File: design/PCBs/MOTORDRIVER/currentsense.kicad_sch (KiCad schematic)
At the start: 0 parts

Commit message: updated PCB
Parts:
- added U5: INA180A1, Package_TO_SOT_SMD:SOT-23-5, symbol Amplifier_Current:INA180A1
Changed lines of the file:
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@@
 	(paper "A4")
 	(rectangle
-		(start 105.41 74.93)
-		(end 162.56 116.84)
+		(start 68.326 64.008)
+		(end 125.476 105.918)
 		(stroke
 			(width 0)
@@
 	(text "Current sensor IC\nTODO: Find component"
 		(exclude_from_sim no)
-		(at 132.334 98.552 0)
+		(at 95.25 87.63 0)
 		(effects
 			(font
@@
 			)
 		)
+	)
+	(symbol
+		(lib_id "Amplifier_Current:INA180A1")
+		(at 153.67 105.41 0)
+		(unit 1)
+		(exclude_from_sim no)
+		(in_bom yes)
+		(on_board yes)
+		(dnp no)
+		(fields_autoplaced yes)
+		(property "Reference" "U5"
+			(at 163.83 98.4755 0)
+			(effects
+				(font
+					(size 1.27 1.27)
+				)
+			)
+		)
+		(property "Value" "INA180A1"
+			(at 163.83 101.0155 0)
+			(effects
+				(font
+					(size 1.27 1.27)
+				)
+			)
+		)
+		(property "Footprint" "Package_TO_SOT_SMD:SOT-23-5"
+			(at 154.94 104.14 0)
+			(effects
+				(font
+					(size 1.27 1.27)
+				)
+				(hide yes)
+			)
+		)
+		(property "Datasheet" "http://www.ti.com/lit/ds/symlink/ina180.pdf"
+			(at 157.48 101.6 0)
+			(effects
+				(font
+					(size 1.27 1.27)
+				)
+				(hide yes)
+			)
+		)
+		(property "Description" "Current Sense Amplifier, 1 Circuit, Rail-to-Rail, 26V, Gain 20 V/V, SOT-23-5"
+			(at 153.67 105.41 0)
+			(effects
+				(font
+					(size 1.27 1.27)
+				)
+				(hide yes)
+			)
+		)
+		(pin "3"
+		)
+		(pin "2"
+		)
+		(pin "1"
+		)
+		(pin "5"
+		)
+		(pin "4"
+		)
+		(instances
+			(project ""
+				(path "/c7634e88-16d1-45ec-9aac-9c841e03cf6d/22c06531-1f6c-46f3-988e-cea008e98016"
+					(reference "U5")
+					(unit 1)
+				)
+				(path "/c7634e88-16d1-45ec-9aac-9c841e03cf6d/474d6285-5514-49ae-8177-1e63fd9cd03e"
+					(reference "U7")
+					(unit 1)
+				)
+				(path "/c7634e88-16d1-45ec-9aac-9c841e03cf6d/721caf15-f1fc-41df-88f3-9bb14360f09a"
+					(reference "U6")
+					(unit 1)
+				)
+			)
+		)

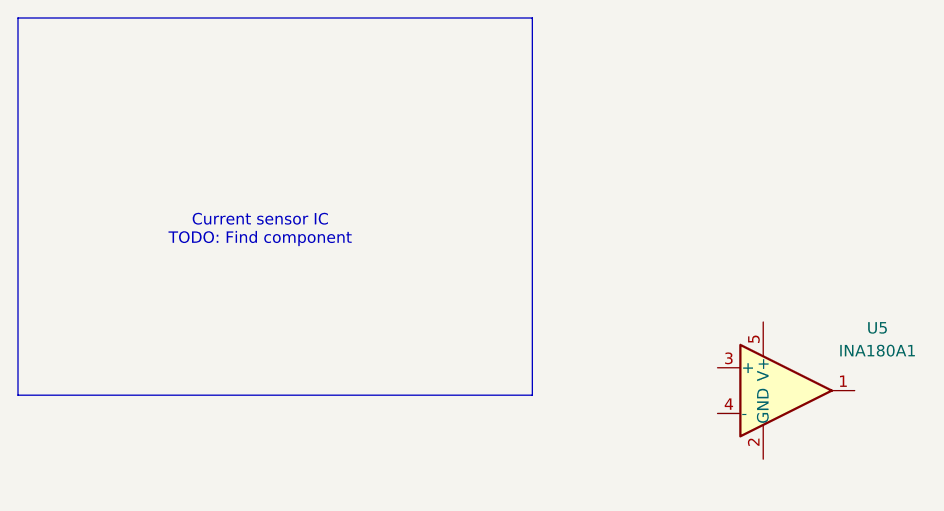
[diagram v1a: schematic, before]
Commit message: fixed schematic layout and added shunt resistor and zener diodes for motor stage
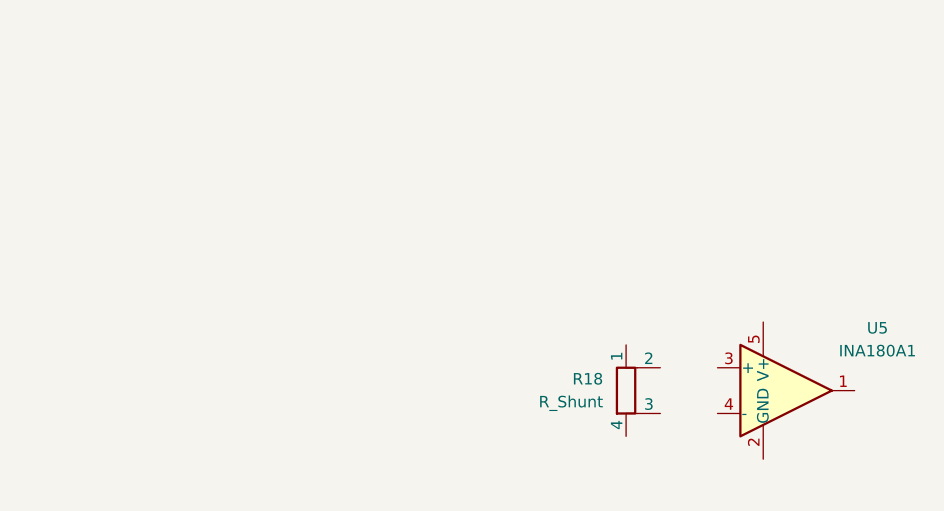
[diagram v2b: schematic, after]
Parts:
- added R18: R_Shunt, symbol Device:R_Shunt
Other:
- note removed: "Current sensor IC TODO: Find component"
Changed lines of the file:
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@@
 	(generator_version "8.0")
 	(paper "A4")
-	(rectangle
-		(start 68.326 64.008)
-		(end 125.476 105.918)
-		(stroke
-			(width 0)
-			(type default)
-		)
-		(fill
-			(type none)
-		)
-	)
-	(text "Current sensor IC\nTODO: Find component"
+	(symbol
+		(lib_id "Device:R_Shunt")
+		(at 135.89 105.41 0)
+		(unit 1)
 		(exclude_from_sim no)
-		(at 95.25 87.63 0)
-		(effects
-			(font
-				(size 1.27 1.27)
+		(in_bom yes)
+		(on_board yes)
+		(dnp no)
+		(fields_autoplaced yes)
+		(property "Reference" "R18"
+			(at 133.35 104.1399 0)
+			(effects
+				(font
+					(size 1.27 1.27)
+				)
+				(justify right)
 			)
 		)
+		(property "Value" "R_Shunt"
+			(at 133.35 106.6799 0)
+			(effects
+				(font
+					(size 1.27 1.27)
+				)
+				(justify right)
+			)
+		)
+		(property "Footprint" ""
+			(at 134.112 105.41 90)
+			(effects
+				(font
+					(size 1.27 1.27)
+				)
+				(hide yes)
+			)
+		)
+		(property "Datasheet" "~"
+			(at 135.89 105.41 0)
+			(effects
+				(font
+					(size 1.27 1.27)
+				)
+				(hide yes)
+			)
+		)
+		(property "Description" "Shunt resistor"
+			(at 135.89 105.41 0)
+			(effects
+				(font
+					(size 1.27 1.27)
+				)
+				(hide yes)
+			)
+		)
+		(pin "1"
+		)
+		(pin "2"
+		)
+		(pin "4"
+		)
+		(pin "3"
+		)
+		(instances
+			(project ""
+				(path "/c7634e88-16d1-45ec-9aac-9c841e03cf6d/22c06531-1f6c-46f3-988e-cea008e98016"
+					(reference "R18")
+					(unit 1)
+				)
+				(path "/c7634e88-16d1-45ec-9aac-9c841e03cf6d/474d6285-5514-49ae-8177-1e63fd9cd03e"
+					(reference "R20")
+					(unit 1)
+				)
+				(path "/c7634e88-16d1-45ec-9aac-9c841e03cf6d/721caf15-f1fc-41df-88f3-9bb14360f09a"
+					(reference "R19")
+					(unit 1)
+				)
+			)
+		)
